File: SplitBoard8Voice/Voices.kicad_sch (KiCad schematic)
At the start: 42 parts, among them J701 VoiceBoardConn_20P_200P, J702 VoiceBoardConn_20P_200P, J703 VoiceBoardConn_20P_200P, J704 VoiceBoardConn_20P_200P, J705 VoiceBoardConn_20P_200P, J706 VoiceBoardConn_20P_200P, U701 TCA9548APWR, U703 L7805, U704 L7905

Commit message: 8 voice schematics start
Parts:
- added J707, J708: VoiceBoardConn_20P_200P, Connector_PinHeader_2.00mm:PinHeader_2x10_P2.00mm_Vertical, symbol Connector_Audio:VoiceBoardConn_20P_200P
- added R717, R718, R719, R720: 2k2, Resistor_SMD:R_0805_2012Metric, symbol Device:R_US
- added TP713: SCL_V7, TestPoint:TestPoint_THTPad_D1.0mm_Drill0.5mm_VAL, symbol Connector:TestPoint
- added TP714: SDA_V7, TestPoint:TestPoint_THTPad_D1.0mm_Drill0.5mm_VAL, symbol Connector:TestPoint
- added TP715: SCL_V8, TestPoint:TestPoint_THTPad_D1.0mm_Drill0.5mm_VAL, symbol Connector:TestPoint
- added TP716: SDA_V8, TestPoint:TestPoint_THTPad_D1.0mm_Drill0.5mm_VAL, symbol Connector:TestPoint
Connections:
- net +12V: now also J707.17 (+12V), J708.17 (+12V)
- net +3.3V: now also J707.15 (+3V3), J708.15 (+3V3), R717.1, R718.1, R719.1, R720.1
- net +5V: now also J707.19 (+5V), J708.19 (+5V)
- net -12V: now also J707.18 (-12V), J708.18 (-12V)
- net -5V: now also J707.20 (-5V), J708.20 (-5V)
- net FOLD_FIRST: now also J707.11 (FF), J708.11 (FF)
- net GND: now also J707.16 (GND), J708.16 (GND)
- net HP_MODE: now also J707.9 (HP), J708.9 (HP)
- net SDA_V7: now reaches U701.17 (SD6)
- net SDA_V7: now also J707.1 (SDA), R718.2, TP714.1
- net SCL_V7: now reaches U701.18 (SC6)
- net SCL_V7: now also J707.3 (SCL), R717.2, TP713.1
- net SDA_V8: now reaches U701.19 (SD7)
- net SDA_V8: now also J708.1 (SDA), R720.2, TP716.1
- net SCL_V8: now reaches U701.20 (SC7)
- net SCL_V8: now also J708.3 (SCL), R719.2, TP715.1
- new net CUTOFF_V7: J707.12 (VCF)
- new net CUTOFF_V8: J708.12 (VCF)
- new net FOLD_V7: J707.10 (FOLD)
- new net FOLD_V8: J708.10 (FOLD)
- new net LVL1_V7: J707.2 (LVL1)
- new net LVL1_V8: J708.2 (LVL1)
- new net LVL2_V7: J707.4 (LVL2)
- new net LVL2_V8: J708.4 (LVL2)
- new net PWM1_V7: J707.6 (PWM1)
- new net PWM1_V8: J708.6 (PWM1)
- new net PWM2_V7: J707.8 (PWM2)
- new net PWM2_V8: J708.8 (PWM2)
- new net V7_CLK1: J707.5 (CLK1)
- new net V7_CLK2: J707.7 (CLK2)
- new net V7_OUT: J707.13 (OUT)
- new net V8_CLK1: J708.5 (CLK1)
- new net V8_CLK2: J708.7 (CLK2)
- new net V8_OUT: J708.13 (OUT)
- new net VCA_V7: J707.14 (VCA)
- new net VCA_V8: J708.14 (VCA)
- no-connect marks 4 -> 0
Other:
- moved on the sheet: C701, J701, J702, J703, J704, J705, J706, R701, R702, R703, R704, R705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

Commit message: galaxy brain clock logic circuit
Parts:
- R702: value 12k -> 10k
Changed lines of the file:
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@@
 			)
 		)
-		(property "Value" "12k"
+		(property "Value" "10k"
 			(at 42.164 88.9 0)
 			(effects

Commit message: 8V layout rev1
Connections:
- net SCL_V1: now also U701.11 (SC3); no longer U701.5 (SC0)
- net SCL_V2: now also U701.9 (SC2); no longer U701.7 (SC1)
- net SCL_V3: now also U701.7 (SC1); no longer U701.9 (SC2)
- net SCL_V4: now also U701.5 (SC0); no longer U701.11 (SC3)
- net SCL_V5: now also U701.20 (SC7); no longer U701.14 (SC4)
- net SCL_V6: now also U701.18 (SC6); no longer U701.16 (SC5)
- net SCL_V7: now also U701.16 (SC5); no longer U701.18 (SC6)
- net SCL_V8: now also U701.14 (SC4); no longer U701.20 (SC7)
- net SDA_V1: now also U701.10 (SD3); no longer U701.4 (SD0)
- net SDA_V2: now also U701.8 (SD2); no longer U701.6 (SD1)
- net SDA_V3: now also U701.6 (SD1); no longer U701.8 (SD2)
- net SDA_V4: now also U701.4 (SD0); no longer U701.10 (SD3)
- net SDA_V5: now also U701.19 (SD7); no longer U701.13 (SD4)
- net SDA_V6: now also U701.17 (SD6); no longer U701.15 (SD5)
- net SDA_V7: now also U701.15 (SD5); no longer U701.17 (SD6)
- net SDA_V8: now also U701.13 (SD4); no longer U701.19 (SD7)
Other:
- moved on the sheet: TP715, TP716
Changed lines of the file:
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@@
 	(wire
 		(pts
-			(xy 29.21 183.388) (xy 29.21 183.134)
+			(xy 27.686 182.372) (xy 27.686 182.118)
 		)
 		(stroke
@@
 	(wire
 		(pts
-			(xy 29.464 190.5) (xy 29.464 190.246)
+			(xy 27.94 189.484) (xy 27.94 189.23)
 		)
 		(stroke
@@
 	(wire
 		(pts
-			(xy 29.464 190.5) (xy 37.084 190.5)
+			(xy 27.94 189.484) (xy 35.56 189.484)
 		)
 		(stroke
@@
 	(wire
 		(pts
-			(xy 29.21 183.388) (xy 36.83 183.388)
+			(xy 27.686 182.372) (xy 35.306 182.372)
 		)
 		(stroke
@@
 	(global_label "SCL_V7"
 		(shape output)
-		(at 87.122 103.632 0)
+		(at 87.122 98.552 0)
 		(fields_autoplaced yes)
 		(effects
@@
 		)
 		(property "Intersheetrefs" "${INTERSHEET_REFS}"
-			(at 96.8805 103.632 0)
+			(at 96.8805 98.552 0)
 			(effects
 				(font
@@
 	(global_label "SCL_V5"
 		(shape output)
-		(at 87.122 93.472 0)
+		(at 87.122 108.712 0)
 		(fields_autoplaced yes)
 		(effects
@@
 		)
 		(property "Intersheetrefs" "${INTERSHEET_REFS}"
-			(at 96.8805 93.472 0)
+			(at 96.8805 108.712 0)
 			(effects
 				(font
@@
 	(global_label "SCL_V2"
 		(shape output)
-		(at 87.122 78.232 0)
+		(at 87.122 83.312 0)
 		(fields_autoplaced yes)
 		(effects
@@
 		)
 		(property "Intersheetrefs" "${INTERSHEET_REFS}"
-			(at 96.8805 78.232 0)
+			(at 96.8805 83.312 0)
 			(effects
 				(font
@@
 	(global_label "SCL_V3"
 		(shape output)
-		(at 87.122 83.312 0)
+		(at 87.122 78.232 0)
 		(fields_autoplaced yes)
 		(effects
@@
 		)
 		(property "Intersheetrefs" "${INTERSHEET_REFS}"
-			(at 96.8805 83.312 0)
+			(at 96.8805 78.232 0)
 			(effects
 				(font
@@
 	(global_label "SDA_V7"
 		(shape output)
-		(at 87.122 106.172 0)
+		(at 87.122 101.092 0)
 		(fields_autoplaced yes)
 		(effects
@@
 		)
 		(property "Intersheetrefs" "${INTERSHEET_REFS}"
-			(at 96.941 106.172 0)
+			(at 96.941 101.092 0)
 			(effects
 				(font
@@
 	(global_label "SDA_V6"
 		(shape output)
-		(at 87.122 101.092 0)
+		(at 87.122 106.172 0)
 		(fields_autoplaced yes)
 		(effects
@@
 		)
 		(property "Intersheetrefs" "${INTERSHEET_REFS}"
-			(at 96.941 101.092 0)
+			(at 96.941 106.172 0)
 			(effects
 				(font
@@
 	(global_label "SCL_V1"
 		(shape output)
-		(at 87.122 73.152 0)
+		(at 87.122 88.392 0)
 		(fields_autoplaced yes)
 		(effects
@@
 		)
 		(property "Intersheetrefs" "${INTERSHEET_REFS}"
-			(at 96.8805 73.152 0)
+			(at 96.8805 88.392 0)
 			(effects
 				(font
@@
 	(global_label "SCL_V6"
 		(shape output)
-		(at 87.122 98.552 0)
+		(at 87.122 103.632 0)
 		(fields_autoplaced yes)
 		(effects
@@
 		)
 		(property "Intersheetrefs" "${INTERSHEET_REFS}"
-			(at 96.8805 98.552 0)
+			(at 96.8805 103.632 0)
 			(effects
 				(font
@@
 	(global_label "SCL_V4"
 		(shape output)
-		(at 87.122 88.392 0)
+		(at 87.122 73.152 0)
 		(fields_autoplaced yes)
 		(effects
@@
 		)
 		(property "Intersheetrefs" "${INTERSHEET_REFS}"
-			(at 96.8805 88.392 0)
+			(at 96.8805 73.152 0)
 			(effects
 				(font
@@
 	(global_label "SCL_V8"
 		(shape input)
-		(at 36.83 183.388 0)
+		(at 35.306 182.372 0)
 		(fields_autoplaced yes)
 		(effects
@@
 		)
 		(property "Intersheetrefs" "${INTERSHEET_REFS}"
-			(at 46.5885 183.388 0)
+			(at 45.0645 182.372 0)
 			(effects
 				(font
@@
 	(global_label "SDA_V8"
 		(shape input)
-		(at 37.084 190.5 0)
+		(at 35.56 189.484 0)
 		(fields_autoplaced yes)
 		(effects
@@
 		)
 		(property "Intersheetrefs" "${INTERSHEET_REFS}"
-			(at 46.903 190.5 0)
+			(at 45.379 189.484 0)
 			(effects
 				(font
@@
 	(global_label "SDA_V4"
 		(shape output)
-		(at 87.122 90.932 0)
+		(at 87.122 75.692 0)
 		(fields_autoplaced yes)
 		(effects
@@
 		)
 		(property "Intersheetrefs" "${INTERSHEET_REFS}"
-			(at 96.941 90.932 0)
+			(at 96.941 75.692 0)
 			(effects
 				(font
@@
 	(global_label "SDA_V5"
 		(shape output)
-		(at 87.122 96.012 0)
+		(at 87.122 111.252 0)
 		(fields_autoplaced yes)
 		(effects
@@
 		)
 		(property "Intersheetrefs" "${INTERSHEET_REFS}"
-			(at 96.941 96.012 0)
+			(at 96.941 111.252 0)
 			(effects
 				(font
@@
 	(global_label "SCL_V8"
 		(shape output)
-		(at 87.122 108.712 0)
+		(at 87.122 93.472 0)
 		(fields_autoplaced yes)
 		(effects
@@
 		)
 		(property "Intersheetrefs" "${INTERSHEET_REFS}"
-			(at 96.8805 108.712 0)
+			(at 96.8805 93.472 0)
 			(effects
 				(font
@@
 	(global_label "SDA_V1"
 		(shape output)
-		(at 87.122 75.692 0)
+		(at 87.122 90.932 0)
 		(fields_autoplaced yes)
 		(effects
@@
 		)
 		(property "Intersheetrefs" "${INTERSHEET_REFS}"
-			(at 96.941 75.692 0)
+			(at 96.941 90.932 0)
 			(effects
 				(font
@@
 	(global_label "SDA_V3"
 		(shape output)
-		(at 87.122 85.852 0)
+		(at 87.122 80.772 0)
 		(fields_autoplaced yes)
 		(effects
@@
 		)
 		(property "Intersheetrefs" "${INTERSHEET_REFS}"
-			(at 96.941 85.852 0)
+			(at 96.941 80.772 0)
 			(effects
 				(font
@@
 	(global_label "SDA_V8"
 		(shape output)
-		(at 87.122 111.252 0)
+		(at 87.122 96.012 0)
 		(fields_autoplaced yes)
 		(effects
@@
 		)
 		(property "Intersheetrefs" "${INTERSHEET_REFS}"
-			(at 96.941 111.252 0)
+			(at 96.941 96.012 0)
 			(effects
 				(font
@@
 	(global_label "SDA_V2"
 		(shape output)
-		(at 87.122 80.772 0)
+		(at 87.122 85.852 0)
 		(fields_autoplaced yes)
 		(effects
@@
 		)
 		(property "Intersheetrefs" "${INTERSHEET_REFS}"
-			(at 96.941 80.772 0)
+			(at 96.941 85.852 0)
 			(effects
 				(font
@@
 	(symbol
 		(lib_id "Connector:TestPoint")
-		(at 29.21 183.134 0)
+		(at 27.686 182.118 0)
 		(unit 1)
 		(exclude_from_sim no)
 		(in_bom no)
-		(on_board yes)
+		(on_board no)
 		(dnp no)
 		(fields_autoplaced yes)
 		(property "Reference" "TP715"
-			(at 31.75 178.5619 0)
+			(at 30.226 177.5459 0)
 			(effects
 				(font
@@
 		)
 		(property "Value" "SCL_V8"
-			(at 31.75 181.1019 0)
+			(at 30.226 180.0859 0)
 			(effects
 				(font
@@
 		)
 		(property "Footprint" "TestPoint:TestPoint_THTPad_D1.0mm_Drill0.5mm_VAL"
-			(at 34.29 183.134 0)
+			(at 32.766 182.118 0)
 			(effects
 				(font
@@
 		)
 		(property "Datasheet" "~"
-			(at 34.29 183.134 0)
+			(at 32.766 182.118 0)
 			(effects
 				(font
@@
 		)
 		(property "Description" "test point"
-			(at 29.21 183.134 0)
+			(at 27.686 182.118 0)
 			(effects
 				(font
@@
 		(exclude_from_sim no)
 		(in_bom no)
-		(on_board yes)
+		(on_board no)
 		(dnp no)
 		(fields_autoplaced yes)
@@
 		(exclude_from_sim no)
 		(in_bom no)
-		(on_board yes)
+		(on_board no)
 		(dnp no)
 		(fields_autoplaced yes)
@@
 		(exclude_from_sim no)
 		(in_bom no)
-		(on_board yes)
+		(on_board no)
 		(dnp no)
 		(fields_autoplaced yes)
@@
 	(symbol
 		(lib_id "Connector:TestPoint")
-		(at 29.464 190.246 0)
+		(at 27.94 189.23 0)
 		(unit 1)
 		(exclude_from_sim no)
 		(in_bom no)
-		(on_board yes)
+		(on_board no)
 		(dnp no)
 		(fields_autoplaced yes)
 		(property "Reference" "TP716"
-			(at 31.75 185.6739 0)
+			(at 30.226 184.6579 0)
 			(effects
 				(font
@@
 		)
 		(property "Value" "SDA_V8"
-			(at 31.75 188.2139 0)
+			(at 30.226 187.1979 0)
 			(effects
 				(font
@@
 		)
 		(property "Footprint" "TestPoint:TestPoint_THTPad_D1.0mm_Drill0.5mm_VAL"
-			(at 34.544 190.246 0)
+			(at 33.02 189.23 0)
 			(effects
 				(font
@@
 		)
 		(property "Datasheet" "~"
-			(at 34.544 190.246 0)
+			(at 33.02 189.23 0)
 			(effects
 				(font
@@
 		)
 		(property "Description" "test point"
-			(at 29.464 190.246 0)
+			(at 27.94 189.23 0)
 			(effects
 				(font
@@
 		(exclude_from_sim no)
 		(in_bom no)
-		(on_board yes)
+		(on_board no)
 		(dnp no)
 		(fields_autoplaced yes)
@@
 		(exclude_from_sim no)
 		(in_bom no)
-		(on_board yes)
+		(on_board no)
 		(dnp no)
 		(fields_autoplaced yes)
@@
 		(exclude_from_sim no)
 		(in_bom no)
-		(on_board yes)
+		(on_board no)
 		(dnp no)
 		(fields_autoplaced yes)
@@
 		(exclude_from_sim no)
 		(in_bom no)
-		(on_board yes)
+		(on_board no)
 		(dnp no)
 		(fields_autoplaced yes)
@@
 		(exclude_from_sim no)
 		(in_bom no)
-		(on_board yes)
+		(on_board no)
 		(dnp no)
 		(fields_autoplaced yes)
@@
 		(exclude_from_sim no)
 		(in_bom no)
-		(on_board yes)
+		(on_board no)
 		(dnp no)
 		(fields_autoplaced yes)
@@
 		(exclude_from_sim no)
 		(in_bom no)
-		(on_board yes)
+		(on_board no)
 		(dnp no)
 		(fields_autoplaced yes)
@@
 		(exclude_from_sim no)
 		(in_bom no)
-		(on_board yes)
+		(on_board no)
 		(dnp no)
 		(fields_autoplaced yes)
@@
 		(exclude_from_sim no)
 		(in_bom no)
-		(on_board yes)
+		(on_board no)
 		(dnp no)
 		(fields_autoplaced yes)
@@
 		(exclude_from_sim no)
 		(in_bom no)
-		(on_board yes)
+		(on_board no)
 		(dnp no)
 		(fields_autoplaced yes)
@@
 		(exclude_from_sim no)
 		(in_bom no)
-		(on_board yes)
+		(on_board no)
 		(dnp no)
 		(fields_autoplaced yes)

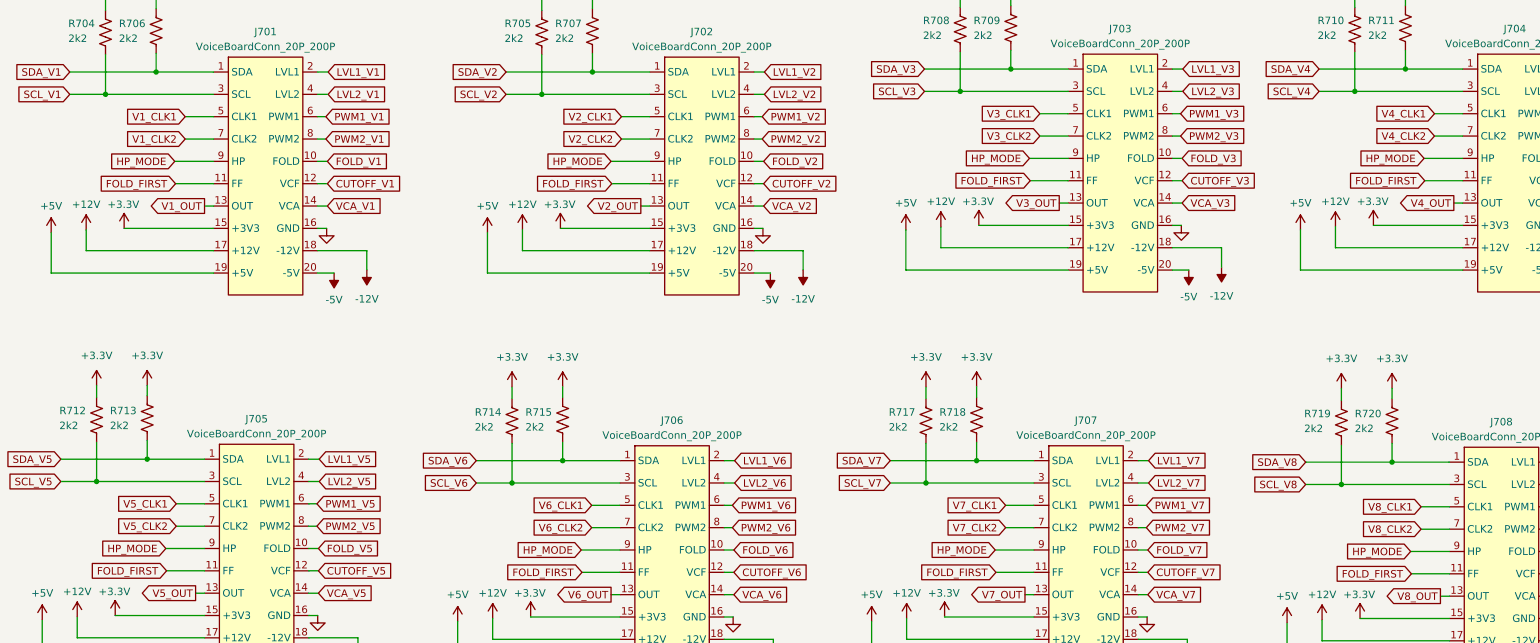
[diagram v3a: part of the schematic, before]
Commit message: some 8voice routing
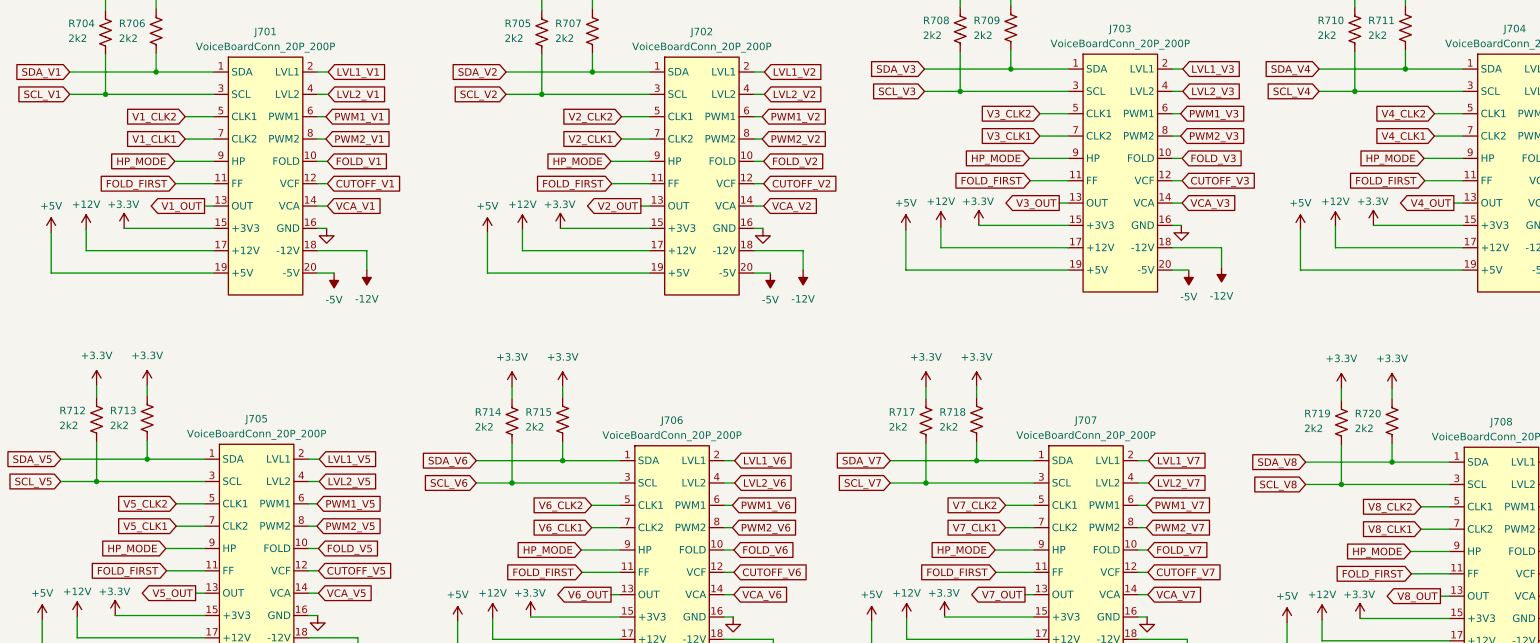
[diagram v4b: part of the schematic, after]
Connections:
- net V1_CLK1: now also J701.7 (CLK2); no longer J701.5 (CLK1)
- net V1_CLK2: now also J701.5 (CLK1); no longer J701.7 (CLK2)
- net V2_CLK1: now also J702.7 (CLK2); no longer J702.5 (CLK1)
- net V2_CLK2: now also J702.5 (CLK1); no longer J702.7 (CLK2)
- net V3_CLK1: now also J703.7 (CLK2); no longer J703.5 (CLK1)
- net V3_CLK2: now also J703.5 (CLK1); no longer J703.7 (CLK2)
- net V4_CLK1: now also J704.7 (CLK2); no longer J704.5 (CLK1)
- net V4_CLK2: now also J704.5 (CLK1); no longer J704.7 (CLK2)
- net V5_CLK1: now also J705.7 (CLK2); no longer J705.5 (CLK1)
- net V5_CLK2: now also J705.5 (CLK1); no longer J705.7 (CLK2)
- net V6_CLK1: now also J706.7 (CLK2); no longer J706.5 (CLK1)
- net V6_CLK2: now also J706.5 (CLK1); no longer J706.7 (CLK2)
- net V7_CLK1: now also J707.7 (CLK2); no longer J707.5 (CLK1)
- net V7_CLK2: now also J707.5 (CLK1); no longer J707.7 (CLK2)
- net V8_CLK1: now also J708.7 (CLK2); no longer J708.5 (CLK1)
- net V8_CLK2: now also J708.5 (CLK1); no longer J708.7 (CLK2)
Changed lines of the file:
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@@
 		)
 	)
-	(global_label "V6_CLK1"
+	(global_label "V6_CLK2"
 		(shape input)
 		(at 223.012 120.904 180)
@@
 		)
 	)
-	(global_label "V6_CLK2"
+	(global_label "V6_CLK1"
 		(shape input)
 		(at 223.012 124.714 180)
@@
 		)
 	)
-	(global_label "V7_CLK2"
+	(global_label "V7_CLK1"
 		(shape input)
 		(at 293.624 124.714 180)
@@
 		)
 	)
-	(global_label "V1_CLK1"
+	(global_label "V1_CLK2"
 		(shape input)
 		(at 153.67 54.61 180)
@@
 		)
 	)
+	(global_label "V8_CLK1"
+		(shape input)
+		(at 364.49 124.968 180)
+		(fields_autoplaced yes)
+		(effects
+			(font
+				(size 1.27 1.27)
+			)
+			(justify right)
+		)
+		(property "Intersheetrefs" "${INTERSHEET_REFS}"
+			(at 353.4615 124.968 0)
+			(effects
+				(font
+					(size 1.27 1.27)
+				)
+				(justify right)
+				(hide yes)
+			)
+		)
+	)
+	(global_label "VCA_V1"
+		(shape input)
+		(at 177.927 69.85 0)
+		(fields_autoplaced yes)
+		(effects
+			(font
+				(size 1.27 1.27)
+			)
+			(justify left)
+		)
+		(property "Intersheetrefs" "${INTERSHEET_REFS}"
+			(at 187.6251 69.85 0)
+			(effects
+				(font
+					(size 1.27 1.27)
+				)
+				(justify left)
+				(hide yes)
+			)
+		)
+	)
 	(global_label "V8_CLK2"
 		(shape input)
-		(at 364.49 124.968 180)
-		(fields_autoplaced yes)
-		(effects
-			(font
-				(size 1.27 1.27)
-			)
-			(justify right)
-		)
-		(property "Intersheetrefs" "${INTERSHEET_REFS}"
-			(at 353.4615 124.968 0)
-			(effects
-				(font
-					(size 1.27 1.27)
-				)
-				(justify right)
-				(hide yes)
-			)
-		)
-	)
-	(global_label "VCA_V1"
-		(shape input)
-		(at 177.927 69.85 0)
-		(fields_autoplaced yes)
-		(effects
-			(font
-				(size 1.27 1.27)
-			)
-			(justify left)
-		)
-		(property "Intersheetrefs" "${INTERSHEET_REFS}"
-			(at 187.6251 69.85 0)
-			(effects
-				(font
-					(size 1.27 1.27)
-				)
-				(justify left)
-				(hide yes)
-			)
-		)
-	)
-	(global_label "V8_CLK1"
-		(shape input)
 		(at 364.49 121.158 180)
 		(fields_autoplaced yes)
@@
 		)
 	)
-	(global_label "V3_CLK1"
+	(global_label "V3_CLK2"
 		(shape input)
 		(at 299.466 54.102 180)
@@
 		)
 	)
-	(global_label "V5_CLK1"
+	(global_label "V5_CLK2"
 		(shape input)
 		(at 152.146 120.65 180)
@@
 		)
 	)
-	(global_label "V4_CLK1"
+	(global_label "V4_CLK2"
 		(shape input)
 		(at 366.776 54.102 180)
@@
 		)
 	)
-	(global_label "V2_CLK2"
+	(global_label "V2_CLK1"
 		(shape input)
 		(at 228.092 58.42 180)
@@
 		)
 	)
-	(global_label "V4_CLK2"
+	(global_label "V4_CLK1"
 		(shape input)
 		(at 366.776 57.912 180)
@@
 		)
 	)
-	(global_label "V3_CLK2"
+	(global_label "V3_CLK1"
 		(shape input)
 		(at 299.466 57.912 180)
@@
 		)
 	)
-	(global_label "V1_CLK2"
+	(global_label "V1_CLK1"
 		(shape input)
 		(at 153.67 58.42 180)
@@
 		)
 	)
-	(global_label "V7_CLK1"
+	(global_label "V7_CLK2"
 		(shape input)
 		(at 293.624 120.904 180)
@@
 		)
 	)
-	(global_label "V2_CLK1"
+	(global_label "V2_CLK2"
 		(shape input)
 		(at 228.092 54.61 180)
@@
 		)
 	)
-	(global_label "V5_CLK2"
+	(global_label "V5_CLK1"
 		(shape input)
 		(at 152.146 124.46 180)
